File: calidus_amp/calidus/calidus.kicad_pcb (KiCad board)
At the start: 2 copper layers, 150 x 120 mm, 127 parts, among them J1 power, J10 led_overload, J11 led_power, J2 input, J3 prevs, J4 icsp, J5 service, J6 sense_bus, J7 left_out, J8 right_out, J9 mute_key, Q1 Q_NPN_CBE, Q2 Q_NPN_CBE, Q3 Q_NPN_CBE, U1 L7805, U2 LM317_3PinPackage, U3 LM337_TO220, U4 TDA7293, U5 TDA7293, U6 PIC18F26K40_ISP

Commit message: WIP: Component placement on PCB
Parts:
- added C41: 100n, Capacitor_THT:C_Rect_L7.0mm_W2.5mm_P5.00mm, F.Cu at (169.1, -34.5)
- added C42: 10u, Capacitor_THT:CP_Radial_D5.0mm_P2.00mm, F.Cu at (177.2, -31.1)
- added R44: 2k4, Resistor_THT:R_Axial_DIN0204_L3.6mm_D1.6mm_P5.08mm_Horizontal, F.Cu at (168.8, -31.9)
- added R45: 10k, Resistor_THT:R_Axial_DIN0204_L3.6mm_D1.6mm_P5.08mm_Horizontal, F.Cu at (176.3, -35.0)
- added R46: 10k, Resistor_THT:R_Axial_DIN0204_L3.6mm_D1.6mm_P5.08mm_Horizontal, F.Cu at (168.8, -29.8)
- C1: value 220n -> 470u; footprint Capacitor_THT:C_Rect_L19.0mm_W8.0mm_P15.00mm_MKS4 -> Capacitor_THT:CP_Radial_D12.5mm_P5.00mm
- C10, C7: value 10u -> 470u; footprint Capacitor_THT:CP_Radial_D5.0mm_P2.00mm -> Capacitor_THT:CP_Radial_D12.5mm_P5.00mm
- C11, C12: value 47u -> 10u; footprint Capacitor_THT:CP_Radial_D10.0mm_P5.00mm -> Capacitor_THT:CP_Radial_D5.0mm_P2.00mm
- C13, C25, C26, C40: value 10u -> 100n; footprint Capacitor_THT:CP_Radial_D5.0mm_P2.00mm -> Capacitor_THT:C_Rect_L7.0mm_W2.5mm_P5.00mm
- C14: value 220u -> 100n; footprint Capacitor_THT:CP_Radial_D6.3mm_P2.50mm -> Capacitor_THT:C_Rect_L7.0mm_W2.5mm_P5.00mm
- C15: value 10u -> 220u; footprint Capacitor_THT:CP_Radial_D5.0mm_P2.00mm -> Capacitor_THT:CP_Radial_D10.0mm_P5.00mm
- C16: value 220u -> 10u; footprint Capacitor_THT:CP_Radial_D6.3mm_P2.50mm -> Capacitor_THT:CP_Radial_D5.0mm_P2.00mm
- C17: value 3p3 -> 10u; footprint Capacitor_THT:C_Disc_D3.0mm_W1.6mm_P2.50mm -> Capacitor_THT:CP_Radial_D5.0mm_P2.00mm
- C18: value 3p3 -> 100n; footprint Capacitor_THT:C_Disc_D3.0mm_W1.6mm_P2.50mm -> Capacitor_THT:C_Rect_L7.0mm_W2.5mm_P5.00mm
- C19: value 47u -> 100n; footprint Capacitor_THT:CP_Radial_D6.3mm_P2.50mm -> Capacitor_THT:C_Rect_L7.0mm_W2.5mm_P5.00mm
- C20: value 47u -> 220u; footprint Capacitor_THT:CP_Radial_D6.3mm_P2.50mm -> Capacitor_THT:CP_Radial_D10.0mm_P5.00mm
- C21, C34: value 100n -> 47u; footprint Capacitor_THT:C_Rect_L7.0mm_W2.5mm_P5.00mm -> Capacitor_THT:CP_Radial_D6.3mm_P2.50mm
- C22: value 100n -> 220p; footprint Capacitor_THT:C_Rect_L7.0mm_W2.5mm_P5.00mm -> Capacitor_THT:C_Disc_D3.0mm_W1.6mm_P2.50mm
- C23: value 100n -> 10u; footprint Capacitor_THT:C_Rect_L7.0mm_W2.5mm_P5.00mm -> Capacitor_THT:CP_Radial_D5.0mm_P2.00mm
- C24: value 100n -> 220u; footprint Capacitor_THT:C_Rect_L7.0mm_W2.5mm_P5.00mm -> Capacitor_THT:CP_Radial_D6.3mm_P2.50mm
- C27, C31: value 100n -> 47u; footprint Capacitor_THT:C_Rect_L7.0mm_W2.5mm_P5.00mm -> Capacitor_THT:CP_Radial_D10.0mm_P5.00mm
- C28: value 100n -> 3p3; footprint Capacitor_THT:C_Rect_L7.0mm_W2.5mm_P5.00mm -> Capacitor_THT:C_Disc_D3.0mm_W1.6mm_P2.50mm
- C35: value 220u -> 220p; footprint Capacitor_THT:CP_Radial_D10.0mm_P5.00mm -> Capacitor_THT:C_Disc_D3.0mm_W1.6mm_P2.50mm
- C36: value 220u -> 10u; footprint Capacitor_THT:CP_Radial_D10.0mm_P5.00mm -> Capacitor_THT:CP_Radial_D5.0mm_P2.00mm
- C37: value 47u -> 220u; footprint Capacitor_THT:CP_Radial_D10.0mm_P5.00mm -> Capacitor_THT:CP_Radial_D6.3mm_P2.50mm
- C38: value 47u -> 3p3; footprint Capacitor_THT:CP_Radial_D10.0mm_P5.00mm -> Capacitor_THT:C_Disc_D3.0mm_W1.6mm_P2.50mm
- C4: value 10m -> 470u; footprint Capacitor_THT:CP_Radial_D30.0mm_P10.00mm_SnapIn -> Capacitor_THT:CP_Radial_D12.5mm_P5.00mm
- C5, C8: value 470u -> 47u; footprint Capacitor_THT:CP_Radial_D12.5mm_P5.00mm -> Capacitor_THT:CP_Radial_D10.0mm_P5.00mm
- C6: value 470u -> 10m; footprint Capacitor_THT:CP_Radial_D12.5mm_P5.00mm -> Capacitor_THT:CP_Radial_D30.0mm_P10.00mm_SnapIn
- C9: value 470u -> 220n; footprint Capacitor_THT:CP_Radial_D12.5mm_P5.00mm -> Capacitor_THT:C_Rect_L19.0mm_W8.0mm_P15.00mm_MKS4
- D1: value D_Bridge_+A-A -> BZX85C20; footprint Diode_THT:Diode_Bridge_32.0x5.6x17.0mm_P10.0mm_P7.5mm -> Diode_THT:D_DO-41_SOD81_P7.62mm_Horizontal
- D10: value MBR1100RLG -> 1N4007
- D11: value MBR1100RLG -> BZX85C20
- D5: value 1N4007 -> MBR1100RLG
- D6: value 1N4007 -> D_Bridge_+A-A; footprint Diode_THT:D_DO-41_SOD81_P7.62mm_Horizontal -> Diode_THT:Diode_Bridge_32.0x5.6x17.0mm_P10.0mm_P7.5mm
- D8: value BZX85C20 -> MBR1100RLG
- D9: value BZX85C20 -> 1N4007
- J1: value power -> left_out; footprint Connector_Phoenix_MC:PhoenixContact_MCV_1,5_3-G-3.5_1x03_P3.50mm_Vertical -> Connector_Phoenix_MC:PhoenixContact_MCV_1,5_2-G-3.5_1x02_P3.50mm_Vertical
- J10: value led_overload -> led_power
- J11: value led_power -> sense_bus; footprint Connector_PinHeader_2.54mm:PinHeader_1x02_P2.54mm_Vertical -> Connector_PinHeader_2.54mm:PinHeader_1x04_P2.54mm_Vertical
- J2: value input -> power
- J3: value prevs -> input
- J4: value icsp -> right_out; footprint Connector_PinHeader_2.54mm:PinHeader_1x06_P2.54mm_Vertical -> Connector_Phoenix_MC:PhoenixContact_MCV_1,5_2-G-3.5_1x02_P3.50mm_Vertical
- J5: value service -> prevs; footprint Connector_PinHeader_2.54mm:PinHeader_1x03_P2.54mm_Vertical -> Connector_Phoenix_MC:PhoenixContact_MCV_1,5_3-G-3.5_1x03_P3.50mm_Vertical
- J6: value sense_bus -> icsp; footprint Connector_PinHeader_2.54mm:PinHeader_1x04_P2.54mm_Vertical -> Connector_PinHeader_2.54mm:PinHeader_1x06_P2.54mm_Vertical
- J7: value left_out -> mute_key; footprint Connector_Phoenix_MC:PhoenixContact_MCV_1,5_2-G-3.5_1x02_P3.50mm_Vertical -> Connector_PinHeader_2.54mm:PinHeader_1x02_P2.54mm_Vertical
- J8: value right_out -> led_overload; footprint Connector_Phoenix_MC:PhoenixContact_MCV_1,5_2-G-3.5_1x02_P3.50mm_Vertical -> Connector_PinHeader_2.54mm:PinHeader_1x02_P2.54mm_Vertical
- J9: value mute_key -> service; footprint Connector_PinHeader_2.54mm:PinHeader_1x02_P2.54mm_Vertical -> Connector_PinHeader_2.54mm:PinHeader_1x03_P2.54mm_Vertical
- R1: value 1 -> 47; footprint Resistor_THT:R_Axial_DIN0207_L6.3mm_D2.5mm_P7.62mm_Horizontal -> Resistor_THT:R_Axial_DIN0309_L9.0mm_D3.2mm_P12.70mm_Horizontal
- R10: value 120 -> 30k
- R12: value 3k3 -> 47
- R15: value 47 -> 10; footprint Resistor_THT:R_Axial_DIN0309_L9.0mm_D3.2mm_P12.70mm_Horizontal -> Resistor_THT:R_Axial_DIN0207_L6.3mm_D2.5mm_P10.16mm_Horizontal
- R16: value 499 -> 10; footprint Resistor_THT:R_Axial_DIN0207_L6.3mm_D2.5mm_P7.62mm_Horizontal -> Resistor_THT:R_Axial_DIN0207_L6.3mm_D2.5mm_P10.16mm_Horizontal
- R17: value 499 -> 20k; footprint Resistor_THT:R_Axial_DIN0207_L6.3mm_D2.5mm_P7.62mm_Horizontal -> Resistor_THT:R_Axial_DIN0204_L3.6mm_D1.6mm_P5.08mm_Horizontal
- R18: value 12k -> 20k; footprint Resistor_THT:R_Axial_DIN0207_L6.3mm_D2.5mm_P10.16mm_Horizontal -> Resistor_THT:R_Axial_DIN0204_L3.6mm_D1.6mm_P5.08mm_Horizontal
- R2: value 1 -> 120; footprint Resistor_THT:R_Axial_DIN0207_L6.3mm_D2.5mm_P7.62mm_Horizontal -> Resistor_THT:R_Axial_DIN0207_L6.3mm_D2.5mm_P10.16mm_Horizontal
- R20: value 12k -> 499; footprint Resistor_THT:R_Axial_DIN0207_L6.3mm_D2.5mm_P10.16mm_Horizontal -> Resistor_THT:R_Axial_DIN0207_L6.3mm_D2.5mm_P7.62mm_Horizontal
- R21: value 12k -> 3.9
- R22: value 3.9 -> 499; footprint Resistor_THT:R_Axial_DIN0207_L6.3mm_D2.5mm_P10.16mm_Horizontal -> Resistor_THT:R_Axial_DIN0207_L6.3mm_D2.5mm_P7.62mm_Horizontal
- R23: value 3.9 -> 12k
- R25: value 3.9 -> 10
- R26: value 10 -> 12k
- R27: value 10 -> 499; footprint Resistor_THT:R_Axial_DIN0207_L6.3mm_D2.5mm_P10.16mm_Horizontal -> Resistor_THT:R_Axial_DIN0207_L6.3mm_D2.5mm_P7.62mm_Horizontal
- R28: value 20k -> 3.9; footprint Resistor_THT:R_Axial_DIN0204_L3.6mm_D1.6mm_P5.08mm_Horizontal -> Resistor_THT:R_Axial_DIN0207_L6.3mm_D2.5mm_P10.16mm_Horizontal
- R29: value 20k -> 499; footprint Resistor_THT:R_Axial_DIN0204_L3.6mm_D1.6mm_P5.08mm_Horizontal -> Resistor_THT:R_Axial_DIN0207_L6.3mm_D2.5mm_P7.62mm_Horizontal
- R3: value 10 -> 47; footprint Resistor_THT:R_Axial_DIN0207_L6.3mm_D2.5mm_P10.16mm_Horizontal -> Resistor_THT:R_Axial_DIN0309_L9.0mm_D3.2mm_P12.70mm_Horizontal
- R30: value 10k -> 12k; footprint Resistor_THT:R_Axial_DIN0204_L3.6mm_D1.6mm_P5.08mm_Horizontal -> Resistor_THT:R_Axial_DIN0207_L6.3mm_D2.5mm_P10.16mm_Horizontal
- R31: value 10k -> 3.9; footprint Resistor_THT:R_Axial_DIN0204_L3.6mm_D1.6mm_P5.08mm_Horizontal -> Resistor_THT:R_Axial_DIN0207_L6.3mm_D2.5mm_P10.16mm_Horizontal
- R32: value 10k -> 10; footprint Resistor_THT:R_Axial_DIN0204_L3.6mm_D1.6mm_P5.08mm_Horizontal -> Resistor_THT:R_Axial_DIN0207_L6.3mm_D2.5mm_P10.16mm_Horizontal
- R33, R34: value 2k4 -> 620
- R35: value 10k -> 620
- R36, R38: value 620 -> 10k
- R4: value 47 -> 1; footprint Resistor_THT:R_Axial_DIN0309_L9.0mm_D3.2mm_P12.70mm_Horizontal -> Resistor_THT:R_Axial_DIN0207_L6.3mm_D2.5mm_P7.62mm_Horizontal
- R41: value 100k -> 10k; footprint Resistor_THT:R_Axial_DIN0207_L6.3mm_D2.5mm_P7.62mm_Horizontal -> Resistor_THT:R_Axial_DIN0204_L3.6mm_D1.6mm_P5.08mm_Horizontal
- R42: value 10k -> 100k; footprint Resistor_THT:R_Axial_DIN0204_L3.6mm_D1.6mm_P5.08mm_Horizontal -> Resistor_THT:R_Axial_DIN0207_L6.3mm_D2.5mm_P7.62mm_Horizontal
- R43: value 620 -> 2k4
- R5: value 47 -> 10k; footprint Resistor_THT:R_Axial_DIN0309_L9.0mm_D3.2mm_P12.70mm_Horizontal -> Resistor_THT:R_Axial_DIN0207_L6.3mm_D2.5mm_P10.16mm_Horizontal
- R6: value 10k -> 30k
- R7: value 10k -> 3k3; footprint Resistor_THT:R_Axial_DIN0207_L6.3mm_D2.5mm_P10.16mm_Horizontal -> Resistor_THT:R_Axial_DIN0309_L9.0mm_D3.2mm_P12.70mm_Horizontal
- R8: value 30k -> 1; footprint Resistor_THT:R_Axial_DIN0207_L6.3mm_D2.5mm_P10.16mm_Horizontal -> Resistor_THT:R_Axial_DIN0207_L6.3mm_D2.5mm_P7.62mm_Horizontal
- R9: value 30k -> 10k
- U1: value L7805 -> LM317_3PinPackage
- U2: value LM317_3PinPackage -> LM337_TO220
- U3: value LM337_TO220 -> L7805
- moved C19 215.5 mm to (324.6, -10.0)
- moved R17 215.5 mm to (347.5, -6.20)
- moved R20 215.5 mm to (337.3, -10.0)
- moved R21 215.5 mm to (337.3, -13.8)
- moved R14 206.9 mm to (107.3, 104.9)
- moved R34 203.9 mm to (271.3, 176.1)
- moved R33 203.9 mm to (296.7, 176.1)
- moved C11 200.5 mm to (296.7, 185.3)
- moved D8 200.5 mm to (308.1, 187.9)
- moved C16 190.9 mm to (327.2, 17.9)
- moved R25 190.9 mm to (370.3, 25.6)
- moved R27 190.9 mm to (370.3, 29.4)
- moved C22 190.9 mm to (364.0, 21.7)
- moved C24 190.9 mm to (356.4, 29.4)
- moved C27 190.9 mm to (294.9, 12.9)
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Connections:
- C1 pad 1: /psupply/pri_hi -> Net-(C1-Pad1)
- C10 pad 1: +pdvs -> Net-(C10-Pad1)
- C10 pad 2: Earth_Protective -> Net-(C10-Pad2)
- C11 pad 1: +vs -> +pwvs
- C12 pad 1: Earth_Protective -> +pdvs
- C12 pad 2: -vs -> Earth_Protective
- C13 pad 1: Net-(C13-Pad1) -> +pwvs
- C13 pad 2: /pamp/in_l -> Earth_Protective
- C14 pad 1: Net-(C14-Pad1) -> +pwvs
- C14 pad 2: GNDS -> Earth_Protective
- C15 pad 1: Net-(C15-Pad1) -> +pwvs
- C15 pad 2: /pamp/in_r -> Earth_Protective
- C16 pad 2: GNDS -> Earth_Protective
- C17 pad 2: Net-(C17-Pad2) -> Earth_Protective
- C18 pad 1: Net-(C18-Pad1) -> Earth_Protective
- C18 pad 2: Net-(C18-Pad2) -> -pwvs
- C19 pad 1: Net-(C19-Pad1) -> Earth_Protective
- C19 pad 2: Net-(C19-Pad2) -> -pwvs
- C2 pad 1: Net-(C2-Pad1) -> /psupply/pri_hi
- C2 pad 2: /Control and Monitoring Unit/ac_in -> Net-(C2-Pad2)
- C20 pad 1: Net-(C20-Pad1) -> Earth_Protective
- C20 pad 2: Net-(C20-Pad2) -> -pwvs
- C21 pad 2: Earth_Protective -> Net-(C21-Pad2)
- C22 pad 2: Earth_Protective -> gnds_l
- C23 pad 2: Earth_Protective -> /pamp/in_l
- C24 pad 2: Earth_Protective -> gnds_l
- C25 pad 1: Net-(C25-Pad1) -> +vs
- C26 pad 1: Net-(C26-Pad1) -> +vs
- C27 pad 1: +pwvs -> +vs
- C28 pad 1: Earth_Protective -> Net-(C28-Pad1)
- C28 pad 2: -pwvs -> Net-(C28-Pad2)
- C29 pad 1: +vs -> Earth_Protective
- C29 pad 2: Earth_Protective -> -vs
- C31 pad 1: +pwvs -> Earth_Protective
- C31 pad 2: Earth_Protective -> -vs
- C32 pad 1: Earth_Protective -> Net-(C32-Pad1)
- C32 pad 2: -pwvs -> Earth_Protective
- C33 pad 1: +vs -> Net-(C33-Pad1)
- C34 pad 1: Earth_Protective -> Net-(C34-Pad1)
- C34 pad 2: -vs -> Net-(C34-Pad2)
- C35 pad 1: +pwvs -> Net-(C35-Pad1)
- C35 pad 2: Earth_Protective -> gnds_r
- C36 pad 1: Earth_Protective -> Net-(C36-Pad1)
- C36 pad 2: -pwvs -> /pamp/in_r
- C37 pad 1: +vs -> Net-(C37-Pad1)
- C37 pad 2: Earth_Protective -> gnds_r
- C38 pad 1: Earth_Protective -> Net-(C38-Pad1)
- C38 pad 2: -vs -> Net-(C38-Pad2)
- C39 pad 1: +pdvs -> Net-(C39-Pad1)
- C4 pad 1: Earth_Protective -> Net-(C4-Pad1)
- C4 pad 2: -pwvs -> Earth_Protective
- C40 pad 1: +pdvs -> Net-(C40-Pad1)
- C5 pad 1: Net-(C5-Pad1) -> +vs
- C5 pad 2: Net-(C5-Pad2) -> Earth_Protective
- C6 pad 1: Net-(C6-Pad1) -> Earth_Protective
- C6 pad 2: Net-(C6-Pad2) -> -pwvs
- C7 pad 1: +pwvs -> Earth_Protective
- C7 pad 2: Earth_Protective -> Net-(C7-Pad2)
- C8 pad 1: Net-(C8-Pad1) -> Earth_Protective
- C8 pad 2: Earth_Protective -> -vs
- C9 pad 1: Earth_Protective -> Net-(C9-Pad1)
- C9 pad 2: Net-(C9-Pad2) -> /Control and Monitoring Unit/ac_in
- D1 pad 1: +pwvs -> Net-(C4-Pad1)
- D1 pad 2: /Control and Monitoring Unit/ac_in -> +vs
- D10 pad 1: +vs -> -vs
- D10 pad 2: +pwvs -> Net-(C7-Pad2)
- D11 pad 1: -pwvs -> -vs
- D11 pad 2: -vs -> Net-(C7-Pad2)
- D12 pad 2: Net-(C17-Pad1) -> Net-(C28-Pad1)
- D13 pad 1: Net-(C17-Pad1) -> Net-(C28-Pad1)
- D14 pad 2: Net-(C18-Pad1) -> Net-(C38-Pad1)
- D15 pad 1: Net-(C18-Pad1) -> Net-(C38-Pad1)
- D2 pad 1: Net-(C5-Pad1) -> Net-(C4-Pad1)
- D2 pad 2: Earth_Protective -> +vs
- D3 pad 1: Earth_Protective -> Net-(C4-Pad1)
- D3 pad 2: Net-(C6-Pad2) -> Net-(C1-Pad1)
- D4 pad 1: Net-(C8-Pad1) -> Net-(C1-Pad1)
- D4 pad 2: Net-(C5-Pad1) -> Earth_Protective
- D5 pad 1: Net-(C6-Pad2) -> +vs
- D5 pad 2: Net-(C9-Pad2) -> +pwvs
- D6 pad 1: Net-(C8-Pad1) -> +pwvs
- D6 pad 2: +vs -> /Control and Monitoring Unit/ac_in
- D7 pad 1: -vs -> Earth_Protective
- D7 pad 2: Net-(C9-Pad2) -> Net-(C10-Pad2)
- D8 pad 1: Net-(C8-Pad1) -> -pwvs
- D8 pad 2: +vs -> -vs
- D9 pad 1: -vs -> Net-(C10-Pad2)
- D9 pad 2: Net-(C9-Pad2) -> Net-(C7-Pad2)
- J1 pad 1: /psupply/pri_hi -> /pamp/out_l
- J10 pad 2: /Control and Monitoring Unit/overload_led -> /Control and Monitoring Unit/power_led
- J11 pad 1: +pdvs -> Earth_Protective
- J11 pad 2: /Control and Monitoring Unit/power_led -> /Control and Monitoring Unit/i2c_scl
- J2 pad 1: /pamp/in_r -> /psupply/pri_hi
- J2 pad 2: GNDS -> Earth_Protective
- J2 pad 3: /pamp/in_l -> /Control and Monitoring Unit/ac_in
- J3 pad 1: -prevs -> /pamp/in_l
- J3 pad 2: Earth_Protective -> gnds_l
- J3 pad 3: +prevs -> /pamp/in_r
- J4 pad 1: /Control and Monitoring Unit/icsprst -> /pamp/out_r
- J4 pad 2: +pdvs -> Earth_Protective
- J5 pad 1: Earth_Protective -> -prevs
- J5 pad 2: /Control and Monitoring Unit/uart_tx -> Earth_Protective
- J5 pad 3: /Control and Monitoring Unit/uart_rx -> +prevs
- J6 pad 1: Earth_Protective -> /Control and Monitoring Unit/icsprst
- J6 pad 2: /Control and Monitoring Unit/i2c_scl -> +pdvs
- J6 pad 3: /Control and Monitoring Unit/i2c_sda -> Earth_Protective
- J6 pad 4: +pdvs -> /Control and Monitoring Unit/icspdat
- J7 pad 1: /pamp/out_l -> +pdvs
- J7 pad 2: Earth_Protective -> /Control and Monitoring Unit/mute_key
- J8 pad 1: /pamp/out_r -> +pdvs
- J8 pad 2: Earth_Protective -> /Control and Monitoring Unit/overload_led
- J9 pad 1: +pdvs -> Earth_Protective
- J9 pad 2: /Control and Monitoring Unit/mute_key -> /Control and Monitoring Unit/uart_tx
- L1 pad 1: Net-(C17-Pad1) -> Net-(C28-Pad1)
- L2 pad 1: Net-(C18-Pad1) -> Net-(C38-Pad1)
- R1 pad 2: Earth_Protective -> /psupply/pri_hi
- R10 pad 1: +vs -> Earth_Protective
- R10 pad 2: Net-(R10-Pad2) -> Net-(C7-Pad2)
- R11 pad 1: Net-(R10-Pad2) -> Earth_Protective
- R11 pad 2: Earth_Protective -> Net-(R11-Pad2)
- R12 pad 1: Earth_Protective -> -prevs
- R12 pad 2: Net-(R12-Pad2) -> -pwvs
- R13 pad 1: Net-(R12-Pad2) -> Net-(R11-Pad2)
- R14 pad 1: +prevs -> Net-(C10-Pad1)
- R14 pad 2: +pwvs -> /Control and Monitoring Unit/ac_in
- R15 pad 1: -prevs -> gnds_l
- R15 pad 2: -pwvs -> Earth_Protective
- R16 pad 1: Net-(C17-Pad2) -> gnds_r
- R16 pad 2: Net-(C14-Pad1) -> Earth_Protective
- R17 pad 1: Net-(C18-Pad2) -> /Control and Monitoring Unit/mute
- R17 pad 2: Net-(C16-Pad1) -> Net-(C17-Pad1)
- R18 pad 1: GNDS -> /Control and Monitoring Unit/stby
- R18 pad 2: Net-(C13-Pad1) -> Net-(C16-Pad1)
- R19 pad 1: Net-(C17-Pad1) -> Net-(C22-Pad1)
- R19 pad 2: Net-(C17-Pad2) -> gnds_l
- R2 pad 1: Earth_Protective -> +vs
- R2 pad 2: Net-(C2-Pad1) -> Net-(R2-Pad2)
- R20 pad 1: GNDS -> Net-(C22-Pad1)
- R20 pad 2: Net-(C15-Pad1) -> Net-(C23-Pad1)
- R21 pad 1: Net-(C18-Pad1) -> /pamp/out_l
- R21 pad 2: Net-(C18-Pad2) -> Net-(C28-Pad1)
- R22 pad 1: Net-(C17-Pad1) -> Net-(C28-Pad2)
- R22 pad 2: Net-(C21-Pad1) -> Net-(C24-Pad1)
- R23 pad 1: Net-(C18-Pad1) -> Net-(C28-Pad1)
- R23 pad 2: Net-(C22-Pad1) -> Net-(C28-Pad2)
- R24 pad 1: /pamp/out_l -> Net-(C28-Pad1)
- R24 pad 2: Net-(C17-Pad1) -> Net-(C32-Pad1)
- R25 pad 1: /pamp/out_r -> /pamp/out_l
- R25 pad 2: Net-(C18-Pad1) -> Net-(C33-Pad1)
- R26 pad 1: /pamp/out_l -> gnds_r
- R26 pad 2: Net-(C23-Pad1) -> Net-(C35-Pad1)
- R27 pad 1: /pamp/out_r -> Net-(C35-Pad1)
- R27 pad 2: Net-(C24-Pad1) -> Net-(C36-Pad1)
- R28 pad 1: /Control and Monitoring Unit/mute -> /pamp/out_r
- R28 pad 2: Net-(C26-Pad1) -> Net-(C38-Pad1)
- R29 pad 1: /Control and Monitoring Unit/stby -> Net-(C38-Pad2)
- R29 pad 2: Net-(C25-Pad1) -> Net-(C37-Pad1)
- R3 pad 1: GNDS -> +prevs
- R3 pad 2: Earth_Protective -> +pwvs
- R30 pad 1: +pdvs -> Net-(C38-Pad1)
- R30 pad 2: /Control and Monitoring Unit/icsprst -> Net-(C38-Pad2)
- R31 pad 1: +pdvs -> Net-(C38-Pad1)
- R31 pad 2: Net-(R31-Pad2) -> Net-(C39-Pad1)
- R32 pad 1: +pdvs -> /pamp/out_r
- R32 pad 2: /Control and Monitoring Unit/overload -> Net-(C40-Pad1)
- R33 pad 1: +pdvs -> Net-(Q1-Pad1)
- R33 pad 2: /Control and Monitoring Unit/i2c_sda -> /Control and Monitoring Unit/power_led
- R34 pad 1: +pdvs -> Net-(Q2-Pad1)
- R34 pad 2: /Control and Monitoring Unit/i2c_scl -> /Control and Monitoring Unit/overload_led
- R35 pad 1: Net-(Q1-Pad2) -> Net-(Q3-Pad1)
- R35 pad 2: Net-(R35-Pad2) -> Net-(D16-Pad1)
- R36 pad 1: Net-(Q1-Pad1) -> +pdvs
- R36 pad 2: /Control and Monitoring Unit/power_led -> /Control and Monitoring Unit/icsprst
- R37 pad 1: Net-(Q2-Pad2) -> +pdvs
- R37 pad 2: /Control and Monitoring Unit/icspclk -> Net-(R37-Pad2)
- R38 pad 1: Net-(Q2-Pad1) -> +pdvs
- R38 pad 2: /Control and Monitoring Unit/overload_led -> /Control and Monitoring Unit/overload
- R39 pad 1: Net-(R39-Pad1) -> Net-(Q1-Pad2)
- R39 pad 2: Earth_Protective -> Net-(R39-Pad2)
- R4 pad 1: Net-(C5-Pad2) -> Net-(C2-Pad2)
- R4 pad 2: /psupply/pri_hi -> Earth_Protective
- R40 pad 1: /Control and Monitoring Unit/mute_key -> Net-(Q2-Pad2)
- R40 pad 2: Earth_Protective -> /Control and Monitoring Unit/icspclk
- R41 pad 1: /Control and Monitoring Unit/ac_in -> Net-(Q3-Pad2)
- R41 pad 2: Net-(R41-Pad2) -> /Control and Monitoring Unit/icspdat
- R42 pad 1: Net-(Q3-Pad2) -> /Control and Monitoring Unit/ac_in
- R42 pad 2: /Control and Monitoring Unit/icspdat -> Net-(R42-Pad2)
- R43 pad 1: Net-(Q3-Pad1) -> +pdvs
- R43 pad 2: Net-(D16-Pad1) -> /Control and Monitoring Unit/i2c_sda
- R5 pad 1: Net-(C6-Pad1) -> +pwvs
- R5 pad 2: /Control and Monitoring Unit/ac_in -> Earth_Protective
- R6 pad 1: +pwvs -> Net-(C4-Pad1)
- R7 pad 1: Earth_Protective -> Net-(R2-Pad2)
- R7 pad 2: -pwvs -> Earth_Protective
- R8 pad 1: Net-(C8-Pad1) -> Earth_Protective
- R8 pad 2: Earth_Protective -> Net-(C9-Pad1)
- R9 pad 2: Net-(C9-Pad2) -> -pwvs
- U1 pad 1: +pwvs -> Net-(R2-Pad2)
- U1 pad 2: Earth_Protective -> +vs
- U1 pad 3: +pdvs -> Net-(C4-Pad1)
- U2 pad 1: Net-(R10-Pad2) -> Net-(R11-Pad2)
- U2 pad 2: +vs -> Net-(C7-Pad2)
- U2 pad 3: Net-(C8-Pad1) -> -vs
- U3 pad 1: Net-(R12-Pad2) -> +pwvs
- U3 pad 2: Net-(C9-Pad2) -> Earth_Protective
- U3 pad 3: -vs -> +pdvs
- U4 pad 10: Net-(C26-Pad1) -> Net-(C17-Pad1)
- U4 pad 12: Net-(C19-Pad2) -> Net-(C21-Pad2)
- U4 pad 14: Net-(C17-Pad1) -> Net-(C28-Pad1)
- U4 pad 2: Net-(C17-Pad2) -> Net-(C28-Pad2)
- U4 pad 3: Net-(C13-Pad1) -> Net-(C22-Pad1)
- U4 pad 4: GNDS -> gnds_l
- U4 pad 6: Net-(C19-Pad1) -> Net-(C21-Pad1)
- U4 pad 9: Net-(C25-Pad1) -> Net-(C16-Pad1)
- U5 pad 10: Net-(C26-Pad1) -> Net-(C17-Pad1)
- U5 pad 12: Net-(C20-Pad2) -> Net-(C34-Pad2)
- U5 pad 14: Net-(C18-Pad1) -> Net-(C38-Pad1)
- U5 pad 2: Net-(C18-Pad2) -> Net-(C38-Pad2)
- U5 pad 3: Net-(C15-Pad1) -> Net-(C35-Pad1)
- U5 pad 4: GNDS -> gnds_r
- U5 pad 6: Net-(C20-Pad1) -> Net-(C34-Pad1)
- U5 pad 9: Net-(C25-Pad1) -> Net-(C16-Pad1)
- U6 pad 11: Net-(R41-Pad2) -> Net-(R42-Pad2)
- U6 pad 13: Net-(R39-Pad1) -> Net-(R45-Pad1)
- U6 pad 21: Net-(R31-Pad2) -> Net-(R37-Pad2)
- U6 pad 26: Net-(R35-Pad2) -> Net-(R39-Pad2)
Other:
- board size 150 x 120 mm -> 140 x 110 mm

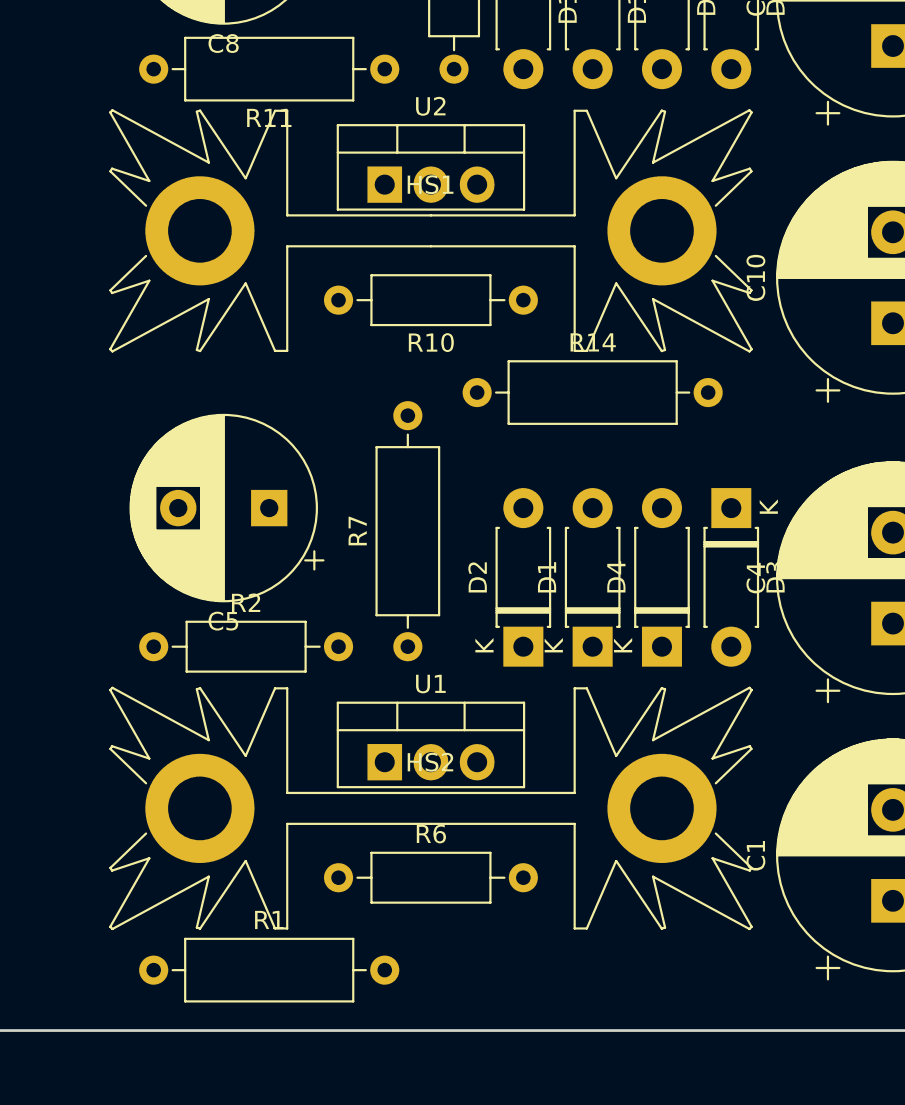
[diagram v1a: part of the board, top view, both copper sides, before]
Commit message: WIP: Removed unnecessary heatsinks
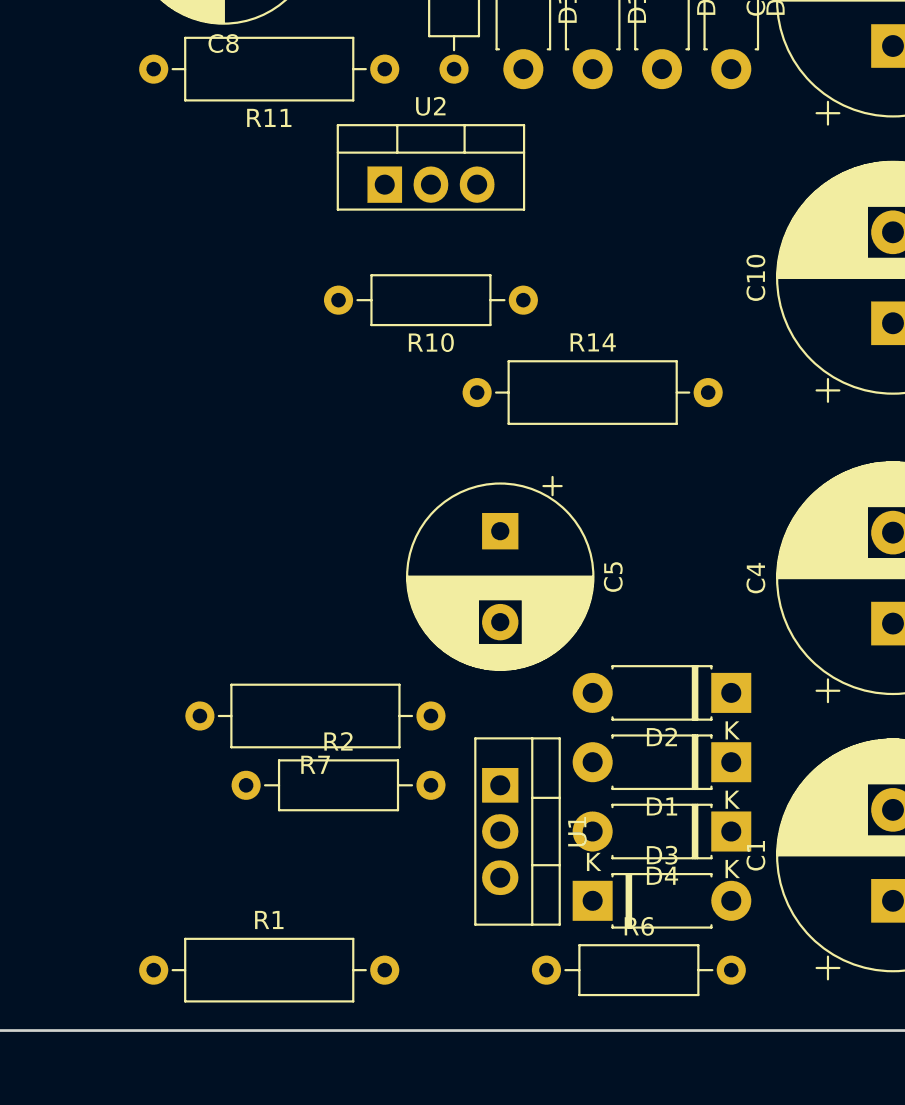
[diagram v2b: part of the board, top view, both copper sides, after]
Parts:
- removed HS1, HS2: Heatsink, Heatsink:Heatsink_Fischer_SK104-STCB_35x13mm__2xDrill3.5mm_ScrewM3
- moved D3 22.9 mm to (113.7, 132.9), turned to 0 degrees
- moved C5 12.8 mm to (108.6, 112.5), turned to 270 degrees
- moved R6 12.5 mm to (111.1, 136.7)
- moved D2 11.7 mm to (121.3, 121.4), turned to 180 degrees
- moved D4 10.9 mm to (121.3, 129.1), turned to 180 degrees
- moved D1 9.92 mm to (121.3, 125.2), turned to 180 degrees
- moved R2 9.16 mm to (94.6, 126.5)
- moved U1 6.48 mm to (108.6, 126.5), turned to 270 degrees
- moved R7 4.02 mm to (104.8, 122.7), turned to 180 degrees

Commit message: WIP: Component placement
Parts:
- added C43: 100n, Capacitor_THT:C_Rect_L7.0mm_W2.5mm_P5.00mm, F.Cu at (56.1, 12.5)
- added C44: 100n, Capacitor_THT:C_Rect_L7.0mm_W2.5mm_P5.00mm, F.Cu at (56.1, 15.5)
- added C45: 100n, Capacitor_THT:C_Rect_L7.0mm_W2.5mm_P5.00mm, F.Cu at (38.7, 12.5)
- added C46: 10u, Capacitor_THT:CP_Radial_D5.0mm_P2.00mm, F.Cu at (46.9, 13.7)
- C16: value 10u -> 220u; footprint Capacitor_THT:CP_Radial_D5.0mm_P2.00mm -> Capacitor_THT:CP_Radial_D10.0mm_P5.00mm
- C18, C25, C40: value 100n -> 10u; footprint Capacitor_THT:C_Rect_L7.0mm_W2.5mm_P5.00mm -> Capacitor_THT:CP_Radial_D5.0mm_P2.00mm
- C20: value 220u -> 100n; footprint Capacitor_THT:CP_Radial_D10.0mm_P5.00mm -> Capacitor_THT:C_Rect_L7.0mm_W2.5mm_P5.00mm
- C21: value 47u -> 220u; footprint Capacitor_THT:CP_Radial_D6.3mm_P2.50mm -> Capacitor_THT:CP_Radial_D10.0mm_P5.00mm
- C22: value 220p -> 220u; footprint Capacitor_THT:C_Disc_D3.0mm_W1.6mm_P2.50mm -> Capacitor_THT:CP_Radial_D10.0mm_P5.00mm
- C23: value 10u -> 47u; footprint Capacitor_THT:CP_Radial_D5.0mm_P2.00mm -> Capacitor_THT:CP_Radial_D6.3mm_P2.50mm
- C24: value 220u -> 220p; footprint Capacitor_THT:CP_Radial_D6.3mm_P2.50mm -> Capacitor_THT:C_Disc_D3.0mm_W1.6mm_P2.50mm
- C26, C41: value 100n -> 220u; footprint Capacitor_THT:C_Rect_L7.0mm_W2.5mm_P5.00mm -> Capacitor_THT:CP_Radial_D6.3mm_P2.50mm
- C27: value 47u -> 100n; footprint Capacitor_THT:CP_Radial_D10.0mm_P5.00mm -> Capacitor_THT:C_Rect_L7.0mm_W2.5mm_P5.00mm
- C28: value 3p3 -> 100n; footprint Capacitor_THT:C_Disc_D3.0mm_W1.6mm_P2.50mm -> Capacitor_THT:C_Rect_L7.0mm_W2.5mm_P5.00mm
- C29, C30: value 100n -> 47u; footprint Capacitor_THT:C_Rect_L7.0mm_W2.5mm_P5.00mm -> Capacitor_THT:CP_Radial_D10.0mm_P5.00mm
- C31: value 47u -> 3p3; footprint Capacitor_THT:CP_Radial_D10.0mm_P5.00mm -> Capacitor_THT:C_Disc_D3.0mm_W1.6mm_P2.50mm
- C34: footprint Capacitor_THT:CP_Radial_D6.3mm_P2.50mm -> Capacitor_THT:CP_Radial_D10.0mm_P5.00mm
- C35: value 220p -> 47u; footprint Capacitor_THT:C_Disc_D3.0mm_W1.6mm_P2.50mm -> Capacitor_THT:CP_Radial_D10.0mm_P5.00mm
- C36: value 10u -> 100n; footprint Capacitor_THT:CP_Radial_D5.0mm_P2.00mm -> Capacitor_THT:C_Rect_L7.0mm_W2.5mm_P5.00mm
- C37: value 220u -> 100n; footprint Capacitor_THT:CP_Radial_D6.3mm_P2.50mm -> Capacitor_THT:C_Rect_L7.0mm_W2.5mm_P5.00mm
- C38: value 3p3 -> 47u; footprint Capacitor_THT:C_Disc_D3.0mm_W1.6mm_P2.50mm -> Capacitor_THT:CP_Radial_D6.3mm_P2.50mm
- C39: value 100n -> 220p; footprint Capacitor_THT:C_Rect_L7.0mm_W2.5mm_P5.00mm -> Capacitor_THT:C_Disc_D3.0mm_W1.6mm_P2.50mm
- C42: value 10u -> 3p3; footprint Capacitor_THT:CP_Radial_D5.0mm_P2.00mm -> Capacitor_THT:C_Disc_D3.0mm_W1.6mm_P2.50mm
- D1, D10, D11, D2, D3, D4, D7, D9: footprint Diode_THT:D_DO-41_SOD81_P7.62mm_Horizontal -> Diode_THT:D_DO-41_SOD81_P10.16mm_Horizontal
- moved C13 291.0 mm to (95.7, 42.7), turned to 270 degrees
- moved R38 285.0 mm to (59.0, 116.4)
- moved C35 270.5 mm to (84.9, 54.8)
- moved C21 261.3 mm to (95.7, 65.6)
- moved C32 258.6 mm to (91.9, 47.8)
- moved R36 253.9 mm to (59.0, 88.4)
- moved R16 241.7 mm to (57.0, 71.3)
- moved C19 232.4 mm to (99.5, 47.8)
- moved C15 225.8 mm to (95.7, 54.8), turned to 0 degrees
- moved R42 222.2 mm to (56.5, 113.8), turned to 0 degrees
- moved R12 221.4 mm to (93.3, 82.1)
- moved C12 215.2 mm to (83.2, 134.1), turned to 270 degrees
- moved C11 212.2 mm to (90.8, 134.1), turned to 270 degrees
- moved C30 211.6 mm to (84.9, 65.6), turned to 0 degrees
- moved C27 209.0 mm to (88.1, 42.7)
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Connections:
- C16 pad 1: Net-(C16-Pad1) -> +pwvs
- C18 pad 1: Earth_Protective -> Net-(C18-Pad1)
- C18 pad 2: -pwvs -> Earth_Protective
- C21 pad 1: Net-(C21-Pad1) -> Earth_Protective
- C21 pad 2: Net-(C21-Pad2) -> -pwvs
- C22 pad 1: Net-(C22-Pad1) -> Earth_Protective
- C22 pad 2: gnds_l -> -pwvs
- C23 pad 2: /pamp/in_l -> Net-(C23-Pad2)
- C25 pad 1: +vs -> Net-(C25-Pad1)
- C25 pad 2: Earth_Protective -> /pamp/in_l
- C26 pad 1: +vs -> Net-(C26-Pad1)
- C26 pad 2: Earth_Protective -> gnds_l
- C28 pad 1: Net-(C28-Pad1) -> +vs
- C28 pad 2: Net-(C28-Pad2) -> Earth_Protective
- C29 pad 1: Earth_Protective -> +vs
- C29 pad 2: -vs -> Earth_Protective
- C30 pad 1: Earth_Protective -> +vs
- C30 pad 2: -vs -> Earth_Protective
- C31 pad 1: Earth_Protective -> Net-(C31-Pad1)
- C31 pad 2: -vs -> Net-(C31-Pad2)
- C32 pad 1: Net-(C32-Pad1) -> Earth_Protective
- C32 pad 2: Earth_Protective -> -vs
- C33 pad 1: Net-(C33-Pad1) -> Earth_Protective
- C33 pad 2: Earth_Protective -> -vs
- C34 pad 1: Net-(C34-Pad1) -> Earth_Protective
- C34 pad 2: Net-(C34-Pad2) -> -vs
- C35 pad 1: Net-(C35-Pad1) -> Earth_Protective
- C35 pad 2: gnds_r -> -vs
- C36 pad 2: /pamp/in_r -> Earth_Protective
- C37 pad 2: gnds_r -> Earth_Protective
- C39 pad 2: Earth_Protective -> gnds_r
- C40 pad 2: Earth_Protective -> /pamp/in_r
- C41 pad 1: +pdvs -> Net-(C41-Pad1)
- C41 pad 2: Earth_Protective -> gnds_r
- C42 pad 1: +pdvs -> Net-(C42-Pad1)
- C42 pad 2: Earth_Protective -> Net-(C42-Pad2)
- D12 pad 2: Net-(C28-Pad1) -> Net-(C31-Pad1)
- D13 pad 1: Net-(C28-Pad1) -> Net-(C31-Pad1)
- D14 pad 2: Net-(C38-Pad1) -> Net-(C42-Pad1)
- D15 pad 1: Net-(C38-Pad1) -> Net-(C42-Pad1)
- L1 pad 1: Net-(C28-Pad1) -> Net-(C31-Pad1)
- L2 pad 1: Net-(C38-Pad1) -> Net-(C42-Pad1)
- R17 pad 2: Net-(C17-Pad1) -> Net-(C18-Pad1)
- R18 pad 2: Net-(C16-Pad1) -> Net-(C17-Pad1)
- R19 pad 1: Net-(C22-Pad1) -> Net-(C24-Pad1)
- R20 pad 1: Net-(C22-Pad1) -> Net-(C24-Pad1)
- R20 pad 2: Net-(C23-Pad1) -> Net-(C25-Pad1)
- R21 pad 2: Net-(C28-Pad1) -> Net-(C31-Pad1)
- R22 pad 1: Net-(C28-Pad2) -> Net-(C31-Pad2)
- R22 pad 2: Net-(C24-Pad1) -> Net-(C26-Pad1)
- R23 pad 1: Net-(C28-Pad1) -> Net-(C31-Pad1)
- R23 pad 2: Net-(C28-Pad2) -> Net-(C31-Pad2)
- R24 pad 1: Net-(C28-Pad1) -> Net-(C31-Pad1)
- R24 pad 2: Net-(C32-Pad1) -> Net-(C36-Pad1)
- R25 pad 2: Net-(C33-Pad1) -> Net-(C37-Pad1)
- R26 pad 2: Net-(C35-Pad1) -> Net-(C39-Pad1)
- R27 pad 1: Net-(C35-Pad1) -> Net-(C39-Pad1)
- R27 pad 2: Net-(C36-Pad1) -> Net-(C40-Pad1)
- R28 pad 2: Net-(C38-Pad1) -> Net-(C42-Pad1)
- R29 pad 1: Net-(C38-Pad2) -> Net-(C42-Pad2)
- R29 pad 2: Net-(C37-Pad1) -> Net-(C41-Pad1)
- R30 pad 1: Net-(C38-Pad1) -> Net-(C42-Pad1)
- R30 pad 2: Net-(C38-Pad2) -> Net-(C42-Pad2)
- R31 pad 1: Net-(C38-Pad1) -> Net-(C42-Pad1)
- R31 pad 2: Net-(C39-Pad1) -> Net-(C43-Pad1)
- R32 pad 2: Net-(C40-Pad1) -> Net-(C44-Pad1)
- U4 pad 10: Net-(C17-Pad1) -> Net-(C18-Pad1)
- U4 pad 12: Net-(C21-Pad2) -> Net-(C23-Pad2)
- U4 pad 14: Net-(C28-Pad1) -> Net-(C31-Pad1)
- U4 pad 2: Net-(C28-Pad2) -> Net-(C31-Pad2)
- U4 pad 3: Net-(C22-Pad1) -> Net-(C24-Pad1)
- U4 pad 6: Net-(C21-Pad1) -> Net-(C23-Pad1)
- U4 pad 9: Net-(C16-Pad1) -> Net-(C17-Pad1)
- U5 pad 10: Net-(C17-Pad1) -> Net-(C18-Pad1)
- U5 pad 12: Net-(C34-Pad2) -> Net-(C38-Pad2)
- U5 pad 14: Net-(C38-Pad1) -> Net-(C42-Pad1)
- U5 pad 2: Net-(C38-Pad2) -> Net-(C42-Pad2)
- U5 pad 3: Net-(C35-Pad1) -> Net-(C39-Pad1)
- U5 pad 6: Net-(C34-Pad1) -> Net-(C38-Pad1)
- U5 pad 9: Net-(C16-Pad1) -> Net-(C17-Pad1)

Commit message: WIP: Component placement
Signed-off-by: Nenad Radulovic <nenad.b.radulovic@gmail.com>
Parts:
- D14, D15: footprint Diode_THT:D_DO-35_SOD27_P10.16mm_Horizontal -> Diode_THT:D_DO-35_SOD27_P7.62mm_Horizontal
- moved R23 294.0 mm to (67.1, 35.1), turned to 0 degrees
- moved C25 280.1 mm to (75.1, 54.1)
- moved C24 279.6 mm to (77.3, 46.5), turned to 180 degrees
- moved C31 271.3 mm to (74.8, 37.6), turned to 0 degrees
- moved R20 266.6 mm to (77.3, 49.0), turned to 180 degrees
- moved R25 261.7 mm to (110.3, 54.8), turned to 270 degrees
- moved C34 258.2 mm to (85.6, 54.8), turned to 0 degrees
- moved C23 253.5 mm to (104.0, 35.1)
- moved C26 244.7 mm to (76.3, 60.5), turned to 180 degrees
- moved R19 242.1 mm to (77.3, 44.0), turned to 180 degrees
- moved R29 241.6 mm to (137.3, 40.2), turned to 180 degrees
- moved R21 234.1 mm to (113.5, 54.8), turned to 270 degrees
- moved R27 233.9 mm to (137.3, 49.0)
- moved C37 230.4 mm to (119.8, 68.1), turned to 180 degrees
- moved R24 229.0 mm to (107.1, 54.8), turned to 270 degrees
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
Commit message: WIP: Component placement and footpring assignment
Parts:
- C29, C30, C34, C35, C5, C8: footprint Capacitor_THT:CP_Radial_D10.0mm_P5.00mm -> Capacitor_THT:CP_Radial_D6.3mm_P2.50mm
- D12, D13: footprint Diode_THT:D_DO-35_SOD27_P10.16mm_Horizontal -> Diode_THT:D_DO-35_SOD27_P7.62mm_Horizontal
- J1, J4: footprint Connector_Phoenix_MC:PhoenixContact_MCV_1,5_2-G-3.5_1x02_P3.50mm_Vertical -> Connector_Phoenix_MC:PhoenixContact_MCV_1,5_2-G-3.81_1x02_P3.81mm_Vertical
- J2: footprint Connector_Phoenix_MC:PhoenixContact_MCV_1,5_3-G-3.5_1x03_P3.50mm_Vertical -> Connector_Phoenix_MC:PhoenixContact_MCV_1,5_3-G-3.81_1x03_P3.81mm_Vertical
- J3: footprint Connector_Phoenix_MC:PhoenixContact_MCV_1,5_3-G-3.5_1x03_P3.50mm_Vertical -> Connector_Phoenix_MC:PhoenixContact_MCV_1,5_4-G-3.5_1x04_P3.50mm_Vertical
- R20, R22, R27, R29: footprint Resistor_THT:R_Axial_DIN0207_L6.3mm_D2.5mm_P7.62mm_Horizontal -> Resistor_THT:R_Axial_DIN0207_L6.3mm_D2.5mm_P10.16mm_Horizontal
- moved D16 312.9 mm to (53.3, 115.1)
- moved R33 249.9 mm to (57.1, 104.9)
- moved R17 242.9 mm to (85.7, 99.8), turned to 0 degrees
- moved C17 229.1 mm to (90.8, 79.5)
- moved C18 227.4 mm to (84.4, 79.5)
- moved R34 217.8 mm to (65.4, 104.9), turned to 180 degrees
- moved J11 217.8 mm to (53.3, 125.9), turned to 90 degrees
- moved J9 214.5 mm to (69.2, 131.0), turned to 90 degrees
- moved R18 213.1 mm to (85.7, 97.3)
- moved R35 211.7 mm to (65.4, 97.3)
- moved J7 184.6 mm to (55.9, 101.1), turned to 270 degrees
- moved J8 183.8 mm to (55.9, 97.9), turned to 270 degrees
- moved J6 183.6 mm to (64.1, 136.7), turned to 90 degrees
- moved J3 183.4 mm to (55.9, 72.6), turned to 90 degrees
- moved Q1 175.3 mm to (61.1, 109.4)
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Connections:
- J3 pad 1: /pamp/in_l -> gnds_r
- J3 pad 2: gnds_l -> /pamp/in_r
- J3 pad 3: /pamp/in_r -> gnds_l
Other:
- copper layers 2 -> 4

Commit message: WIP: Component placement and footprint assignement
- Finished all capacitors
- Finished all ICs
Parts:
- C13, C14, C19, C20, C27, C28, C32, C33, C36, C43, C45: footprint Capacitor_THT:C_Rect_L7.0mm_W2.5mm_P5.00mm -> Capacitor_THT:C_Rect_L4.6mm_W3.0mm_P2.50mm_MKS02_FKP02
- C24, C31, C39, C42: footprint Capacitor_THT:C_Disc_D3.0mm_W1.6mm_P2.50mm -> Capacitor_THT:C_Disc_D3.8mm_W2.6mm_P2.50mm
- C37, C44: footprint Capacitor_THT:C_Rect_L7.0mm_W2.5mm_P5.00mm -> Capacitor_THT:C_Disc_D5.1mm_W3.2mm_P5.00mm
- R42: footprint Resistor_THT:R_Axial_DIN0207_L6.3mm_D2.5mm_P7.62mm_Horizontal -> Resistor_THT:R_Axial_DIN0204_L3.6mm_D1.6mm_P5.08mm_Horizontal
- U1: value LM317_3PinPackage -> LM317
- U2: value LM337_TO220 -> LM337
- U6: value PIC18F26K40_ISP -> PIC18F26K42-I/SP
- moved C37 6.35 mm to (113.5, 68.1), turned to 0 degrees
- moved C44 6.35 mm to (173.5, 68.1), turned to 0 degrees
- moved C29 3.24 mm to (88.1, 57.3)
- moved C35 3.17 mm to (148.1, 57.3)
- moved C15 2.84 mm to (95.7, 52.2)
- moved C21 2.84 mm to (95.7, 63.0)
- moved C16 2.62 mm to (160.8, 52.2)
- moved C22 2.62 mm to (160.8, 63.0)
- moved C34 2.62 mm to (88.1, 50.3)
- moved C30 2.54 mm to (148.1, 50.3)
- moved C19 2.50 mm to (99.5, 45.2)
- moved C20 2.50 mm to (159.5, 45.2)
- moved C32 2.50 mm to (91.9, 45.2)
- moved C33 2.50 mm to (151.9, 45.2)
- moved C25 2.45 mm to (70.0, 55.3)
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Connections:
- R23 pad 1: Net-(C31-Pad1) -> Net-(C31-Pad2)
- R23 pad 2: Net-(C31-Pad2) -> Net-(C31-Pad1)
- R26 pad 1: gnds_r -> Net-(C39-Pad1)
- R26 pad 2: Net-(C39-Pad1) -> gnds_r
- R30 pad 1: Net-(C42-Pad1) -> Net-(C42-Pad2)
- R30 pad 2: Net-(C42-Pad2) -> Net-(C42-Pad1)
